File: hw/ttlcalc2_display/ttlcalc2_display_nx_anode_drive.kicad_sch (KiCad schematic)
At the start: 89 parts, among them Q26 MPSA92, Q27 MPSA92, Q28 MPSA92, Q29 MPSA92, Q30 MPSA92, Q31 MPSA42, Q32 MPSA42, Q33 MPSA42, Q34 MPSA42, Q35 MPSA42, Q36 MPSA92, Q37 MPSA92, Q38 MPSA92, Q39 MPSA92, Q40 MPSA92, Q41 MPSA42, Q42 MPSA42, Q43 MPSA42, Q44 MPSA42, Q45 MPSA42, Q46 MPSA92, Q47 MPSA92, Q48 MPSA92, Q49 MPSA92, Q50 MPSA42, Q51 MPSA42, Q52 MPSA42, Q53 MPSA42, U14 74LS04, U15 74LS138, U16 74LS138, U17 74LS04, U18 74LS04

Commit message: Continue work on display driver board schematic
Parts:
- R28: renamed from R43; footprint Resistor_THT:R_Axial_DIN0309_L9.0mm_D3.2mm_P2.54mm_Vertical -> Resistor_THT:R_Axial_DIN0207_L6.3mm_D2.5mm_P2.54mm_Vertical
- R29: renamed from R63; footprint Resistor_THT:R_Axial_DIN0309_L9.0mm_D3.2mm_P2.54mm_Vertical -> Resistor_THT:R_Axial_DIN0207_L6.3mm_D2.5mm_P2.54mm_Vertical
- R30: renamed from R80; footprint Resistor_THT:R_Axial_DIN0309_L9.0mm_D3.2mm_P2.54mm_Vertical -> Resistor_THT:R_Axial_DIN0207_L6.3mm_D2.5mm_P2.54mm_Vertical
- R31: renamed from R28; footprint Resistor_THT:R_Axial_DIN0309_L9.0mm_D3.2mm_P2.54mm_Vertical -> Resistor_THT:R_Axial_DIN0207_L6.3mm_D2.5mm_P2.54mm_Vertical
- R32: renamed from R33; footprint Resistor_THT:R_Axial_DIN0309_L9.0mm_D3.2mm_P2.54mm_Vertical -> Resistor_THT:R_Axial_DIN0207_L6.3mm_D2.5mm_P2.54mm_Vertical
- R33: renamed from R48; footprint Resistor_THT:R_Axial_DIN0309_L9.0mm_D3.2mm_P2.54mm_Vertical -> Resistor_THT:R_Axial_DIN0207_L6.3mm_D2.5mm_P2.54mm_Vertical
- R34: renamed from R53; footprint Resistor_THT:R_Axial_DIN0309_L9.0mm_D3.2mm_P2.54mm_Vertical -> Resistor_THT:R_Axial_DIN0207_L6.3mm_D2.5mm_P2.54mm_Vertical
- R35: renamed from R68; footprint Resistor_THT:R_Axial_DIN0309_L9.0mm_D3.2mm_P2.54mm_Vertical -> Resistor_THT:R_Axial_DIN0207_L6.3mm_D2.5mm_P2.54mm_Vertical
- R36: renamed from R72; footprint Resistor_THT:R_Axial_DIN0309_L9.0mm_D3.2mm_P2.54mm_Vertical -> Resistor_THT:R_Axial_DIN0207_L6.3mm_D2.5mm_P2.54mm_Vertical
- R37: renamed from R38; footprint Resistor_THT:R_Axial_DIN0309_L9.0mm_D3.2mm_P2.54mm_Vertical -> Resistor_THT:R_Axial_DIN0207_L6.3mm_D2.5mm_P2.54mm_Vertical
- R38: renamed from R58; footprint Resistor_THT:R_Axial_DIN0309_L9.0mm_D3.2mm_P2.54mm_Vertical -> Resistor_THT:R_Axial_DIN0207_L6.3mm_D2.5mm_P2.54mm_Vertical
- R39: renamed from R76; footprint Resistor_THT:R_Axial_DIN0309_L9.0mm_D3.2mm_P2.54mm_Vertical -> Resistor_THT:R_Axial_DIN0207_L6.3mm_D2.5mm_P2.54mm_Vertical
- R40: renamed from R44; footprint Resistor_THT:R_Axial_DIN0309_L9.0mm_D3.2mm_P2.54mm_Vertical -> Resistor_THT:R_Axial_DIN0207_L6.3mm_D2.5mm_P2.54mm_Vertical
- R41: renamed from R64; footprint Resistor_THT:R_Axial_DIN0309_L9.0mm_D3.2mm_P2.54mm_Vertical -> Resistor_THT:R_Axial_DIN0207_L6.3mm_D2.5mm_P2.54mm_Vertical
- R42: renamed from R81; footprint Resistor_THT:R_Axial_DIN0309_L9.0mm_D3.2mm_P2.54mm_Vertical -> Resistor_THT:R_Axial_DIN0207_L6.3mm_D2.5mm_P2.54mm_Vertical
- R43: renamed from R29; footprint Resistor_THT:R_Axial_DIN0309_L9.0mm_D3.2mm_P2.54mm_Vertical -> Resistor_THT:R_Axial_DIN0207_L6.3mm_D2.5mm_P2.54mm_Vertical
- R44: renamed from R34; footprint Resistor_THT:R_Axial_DIN0309_L9.0mm_D3.2mm_P2.54mm_Vertical -> Resistor_THT:R_Axial_DIN0207_L6.3mm_D2.5mm_P2.54mm_Vertical
- R45: renamed from R49; footprint Resistor_THT:R_Axial_DIN0309_L9.0mm_D3.2mm_P2.54mm_Vertical -> Resistor_THT:R_Axial_DIN0207_L6.3mm_D2.5mm_P2.54mm_Vertical
- R46: renamed from R54; footprint Resistor_THT:R_Axial_DIN0309_L9.0mm_D3.2mm_P2.54mm_Vertical -> Resistor_THT:R_Axial_DIN0207_L6.3mm_D2.5mm_P2.54mm_Vertical
- R47: renamed from R69; footprint Resistor_THT:R_Axial_DIN0309_L9.0mm_D3.2mm_P2.54mm_Vertical -> Resistor_THT:R_Axial_DIN0207_L6.3mm_D2.5mm_P2.54mm_Vertical
- R48: renamed from R73; footprint Resistor_THT:R_Axial_DIN0309_L9.0mm_D3.2mm_P2.54mm_Vertical -> Resistor_THT:R_Axial_DIN0207_L6.3mm_D2.5mm_P2.54mm_Vertical
- R49: renamed from R39; footprint Resistor_THT:R_Axial_DIN0309_L9.0mm_D3.2mm_P2.54mm_Vertical -> Resistor_THT:R_Axial_DIN0207_L6.3mm_D2.5mm_P2.54mm_Vertical
- R50: renamed from R59; footprint Resistor_THT:R_Axial_DIN0309_L9.0mm_D3.2mm_P2.54mm_Vertical -> Resistor_THT:R_Axial_DIN0207_L6.3mm_D2.5mm_P2.54mm_Vertical
- R51: renamed from R77; footprint Resistor_THT:R_Axial_DIN0309_L9.0mm_D3.2mm_P2.54mm_Vertical -> Resistor_THT:R_Axial_DIN0207_L6.3mm_D2.5mm_P2.54mm_Vertical
- R52: renamed from R45; footprint Resistor_THT:R_Axial_DIN0309_L9.0mm_D3.2mm_P2.54mm_Vertical -> Resistor_THT:R_Axial_DIN0207_L6.3mm_D2.5mm_P2.54mm_Vertical
- R53: renamed from R65; footprint Resistor_THT:R_Axial_DIN0309_L9.0mm_D3.2mm_P2.54mm_Vertical -> Resistor_THT:R_Axial_DIN0207_L6.3mm_D2.5mm_P2.54mm_Vertical
- R54: renamed from R82; footprint Resistor_THT:R_Axial_DIN0309_L9.0mm_D3.2mm_P2.54mm_Vertical -> Resistor_THT:R_Axial_DIN0207_L6.3mm_D2.5mm_P2.54mm_Vertical
- R55: renamed from R30; footprint Resistor_THT:R_Axial_DIN0309_L9.0mm_D3.2mm_P2.54mm_Vertical -> Resistor_THT:R_Axial_DIN0207_L6.3mm_D2.5mm_P2.54mm_Vertical
- R56: renamed from R35; footprint Resistor_THT:R_Axial_DIN0309_L9.0mm_D3.2mm_P2.54mm_Vertical -> Resistor_THT:R_Axial_DIN0207_L6.3mm_D2.5mm_P2.54mm_Vertical
- R57: renamed from R50; footprint Resistor_THT:R_Axial_DIN0309_L9.0mm_D3.2mm_P2.54mm_Vertical -> Resistor_THT:R_Axial_DIN0207_L6.3mm_D2.5mm_P2.54mm_Vertical
- R58: renamed from R55; footprint Resistor_THT:R_Axial_DIN0309_L9.0mm_D3.2mm_P2.54mm_Vertical -> Resistor_THT:R_Axial_DIN0207_L6.3mm_D2.5mm_P2.54mm_Vertical
- R59: renamed from R70; footprint Resistor_THT:R_Axial_DIN0309_L9.0mm_D3.2mm_P2.54mm_Vertical -> Resistor_THT:R_Axial_DIN0207_L6.3mm_D2.5mm_P2.54mm_Vertical
- R60: renamed from R74; footprint Resistor_THT:R_Axial_DIN0309_L9.0mm_D3.2mm_P2.54mm_Vertical -> Resistor_THT:R_Axial_DIN0207_L6.3mm_D2.5mm_P2.54mm_Vertical
- R61: renamed from R40; footprint Resistor_THT:R_Axial_DIN0309_L9.0mm_D3.2mm_P2.54mm_Vertical -> Resistor_THT:R_Axial_DIN0207_L6.3mm_D2.5mm_P2.54mm_Vertical
- R62: renamed from R60; footprint Resistor_THT:R_Axial_DIN0309_L9.0mm_D3.2mm_P2.54mm_Vertical -> Resistor_THT:R_Axial_DIN0207_L6.3mm_D2.5mm_P2.54mm_Vertical
- R63: renamed from R78; footprint Resistor_THT:R_Axial_DIN0309_L9.0mm_D3.2mm_P2.54mm_Vertical -> Resistor_THT:R_Axial_DIN0207_L6.3mm_D2.5mm_P2.54mm_Vertical
- R64: renamed from R46; footprint Resistor_THT:R_Axial_DIN0309_L9.0mm_D3.2mm_P2.54mm_Vertical -> Resistor_THT:R_Axial_DIN0207_L6.3mm_D2.5mm_P2.54mm_Vertical
- R65: renamed from R66; footprint Resistor_THT:R_Axial_DIN0309_L9.0mm_D3.2mm_P2.54mm_Vertical -> Resistor_THT:R_Axial_DIN0207_L6.3mm_D2.5mm_P2.54mm_Vertical
- R66: renamed from R83; footprint Resistor_THT:R_Axial_DIN0309_L9.0mm_D3.2mm_P2.54mm_Vertical -> Resistor_THT:R_Axial_DIN0207_L6.3mm_D2.5mm_P2.54mm_Vertical
- R67: renamed from R31; footprint Resistor_THT:R_Axial_DIN0309_L9.0mm_D3.2mm_P2.54mm_Vertical -> Resistor_THT:R_Axial_DIN0207_L6.3mm_D2.5mm_P2.54mm_Vertical
- R68: renamed from R36; footprint Resistor_THT:R_Axial_DIN0309_L9.0mm_D3.2mm_P2.54mm_Vertical -> Resistor_THT:R_Axial_DIN0207_L6.3mm_D2.5mm_P2.54mm_Vertical
- R69: renamed from R51; footprint Resistor_THT:R_Axial_DIN0309_L9.0mm_D3.2mm_P2.54mm_Vertical -> Resistor_THT:R_Axial_DIN0207_L6.3mm_D2.5mm_P2.54mm_Vertical
- R70: renamed from R56; footprint Resistor_THT:R_Axial_DIN0309_L9.0mm_D3.2mm_P2.54mm_Vertical -> Resistor_THT:R_Axial_DIN0207_L6.3mm_D2.5mm_P2.54mm_Vertical
- R71: footprint Resistor_THT:R_Axial_DIN0309_L9.0mm_D3.2mm_P2.54mm_Vertical -> Resistor_THT:R_Axial_DIN0207_L6.3mm_D2.5mm_P2.54mm_Vertical
- R72: renamed from R75; footprint Resistor_THT:R_Axial_DIN0309_L9.0mm_D3.2mm_P2.54mm_Vertical -> Resistor_THT:R_Axial_DIN0207_L6.3mm_D2.5mm_P2.54mm_Vertical
- R73: renamed from R41; footprint Resistor_THT:R_Axial_DIN0309_L9.0mm_D3.2mm_P2.54mm_Vertical -> Resistor_THT:R_Axial_DIN0207_L6.3mm_D2.5mm_P2.54mm_Vertical
- R74: renamed from R61; footprint Resistor_THT:R_Axial_DIN0309_L9.0mm_D3.2mm_P2.54mm_Vertical -> Resistor_THT:R_Axial_DIN0207_L6.3mm_D2.5mm_P2.54mm_Vertical
- R75: renamed from R79; footprint Resistor_THT:R_Axial_DIN0309_L9.0mm_D3.2mm_P2.54mm_Vertical -> Resistor_THT:R_Axial_DIN0207_L6.3mm_D2.5mm_P2.54mm_Vertical
- R76: renamed from R47; footprint Resistor_THT:R_Axial_DIN0309_L9.0mm_D3.2mm_P2.54mm_Vertical -> Resistor_THT:R_Axial_DIN0207_L6.3mm_D2.5mm_P2.54mm_Vertical
- R77: renamed from R67; footprint Resistor_THT:R_Axial_DIN0309_L9.0mm_D3.2mm_P2.54mm_Vertical -> Resistor_THT:R_Axial_DIN0207_L6.3mm_D2.5mm_P2.54mm_Vertical
- R78: renamed from R32; footprint Resistor_THT:R_Axial_DIN0309_L9.0mm_D3.2mm_P2.54mm_Vertical -> Resistor_THT:R_Axial_DIN0207_L6.3mm_D2.5mm_P2.54mm_Vertical
- R79: renamed from R37; footprint Resistor_THT:R_Axial_DIN0309_L9.0mm_D3.2mm_P2.54mm_Vertical -> Resistor_THT:R_Axial_DIN0207_L6.3mm_D2.5mm_P2.54mm_Vertical
- R80: renamed from R52; footprint Resistor_THT:R_Axial_DIN0309_L9.0mm_D3.2mm_P2.54mm_Vertical -> Resistor_THT:R_Axial_DIN0207_L6.3mm_D2.5mm_P2.54mm_Vertical
- R81: renamed from R57; footprint Resistor_THT:R_Axial_DIN0309_L9.0mm_D3.2mm_P2.54mm_Vertical -> Resistor_THT:R_Axial_DIN0207_L6.3mm_D2.5mm_P2.54mm_Vertical
- R82: renamed from R42; footprint Resistor_THT:R_Axial_DIN0309_L9.0mm_D3.2mm_P2.54mm_Vertical -> Resistor_THT:R_Axial_DIN0207_L6.3mm_D2.5mm_P2.54mm_Vertical
- R83: renamed from R62; footprint Resistor_THT:R_Axial_DIN0309_L9.0mm_D3.2mm_P2.54mm_Vertical -> Resistor_THT:R_Axial_DIN0207_L6.3mm_D2.5mm_P2.54mm_Vertical
- renumbered Q31 to Q26, Q41 to Q27, Q50 to Q28, Q26 to Q29, Q36 to Q30, Q46 to Q31, Q42 to Q33, Q51 to Q34, Q27 to Q35, Q37 to Q36, Q47 to Q37, Q33 to Q38, Q43 to Q39, Q52 to Q40, Q28 to Q41, Q38 to Q42, Q48 to Q43, Q34 to Q44, Q44 to Q45, Q53 to Q46, Q29 to Q47, Q39 to Q48, Q35 to Q50, Q45 to Q51, Q30 to Q52, Q40 to Q53

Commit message: Simplify display driver board, add busy light
Removed digit storage and multiplexing logic from display driver, will handle in software instead
Add driver for busy indicator
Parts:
- renumbered Q26 to Q27, Q27 to Q28, Q28 to Q29, Q29 to Q30, Q30 to Q31, Q31 to Q32, Q32 to Q33, Q33 to Q34, Q34 to Q35, Q35 to Q36, Q36 to Q37, Q37 to Q38, Q38 to Q39, Q39 to Q40, Q40 to Q41, Q41 to Q42, Q42 to Q43, Q43 to Q44, Q44 to Q45, Q45 to Q46, Q46 to Q47, Q47 to Q48, Q48 to Q49, Q49 to Q50, Q50 to Q51, Q51 to Q52, Q52 to Q53, Q53 to Q54, R28 to R27, R29 to R28, R30 to R29, R31 to R30, R32 to R31, R33 to R32, R34 to R33, R35 to R34, R36 to R35, R37 to R36, R38 to R37, R39 to R38, R40 to R39, R41 to R40, R42 to R41, R43 to R42, R44 to R43, R45 to R44, R46 to R45, R47 to R46, R48 to R47, R49 to R48, R50 to R49, R51 to R50, R52 to R51, R53 to R52, R54 to R53, R55 to R54, R56 to R55, R57 to R56, R58 to R57, R59 to R58, R60 to R59, R61 to R60, R62 to R61, R63 to R62, R64 to R63, R65 to R64, R66 to R65, R67 to R66, R68 to R67, R69 to R68, R70 to R69, R71 to R70, R72 to R71, R73 to R72, R74 to R73, R75 to R74, R76 to R75, R77 to R76, R78 to R77, R79 to R78, R80 to R79, R81 to R80, R82 to R81, R83 to R82
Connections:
- net EN2 is gone; now on net VCC: U15.6 (E3)
- net GND: no longer U16.5 (E2)
- net ~{EN1} renamed ~{EN}
- net ~{EN}: now also U16.5 (E2)

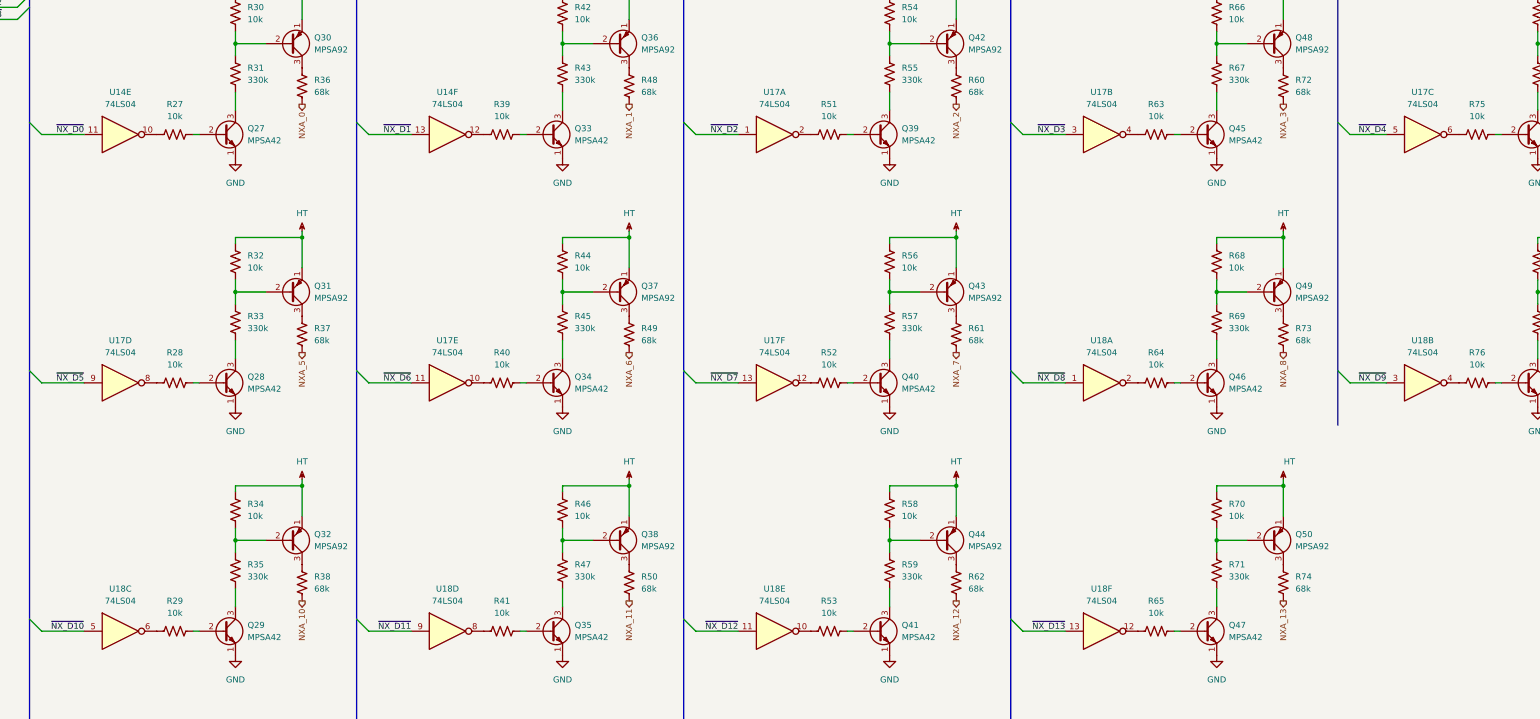
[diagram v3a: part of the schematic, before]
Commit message: Display driver board routing and silkscreen tweaks
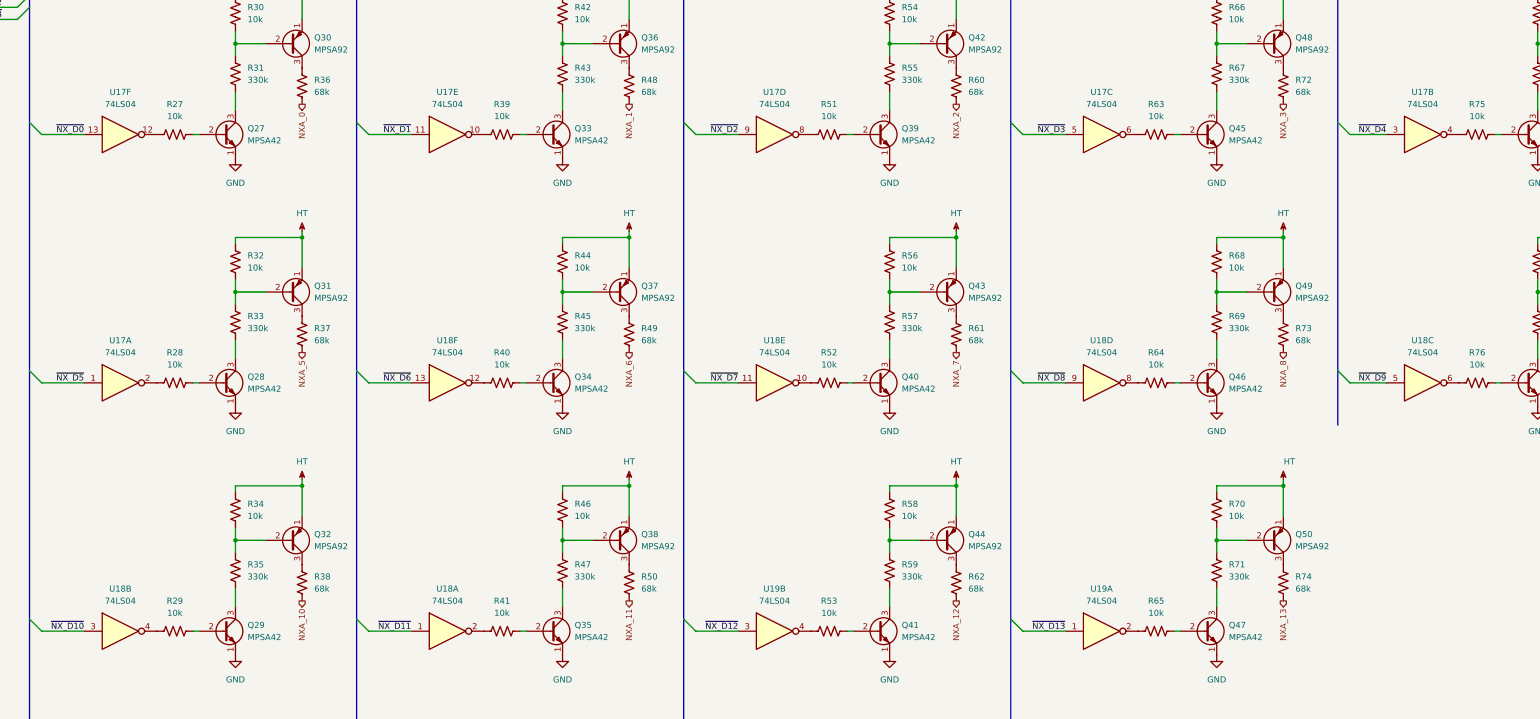
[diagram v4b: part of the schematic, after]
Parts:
- removed unit 2 of U17
- removed unit 3 of U17
- added U19: 74LS04, Package_DIP:DIP-14_W7.62mm, symbol 74xx:74LS04
- Q27, Q28, Q29, Q30, Q31, Q32, Q33, Q34, Q35, Q36, Q37, Q38, Q39, Q40, Q41, Q42, Q43, Q44, Q45, Q46, Q47, Q48, Q49, Q50, Q51, Q52, Q53, Q54: footprint Package_TO_SOT_THT:TO-92_Inline -> Package_TO_SOT_THT:TO-92_Inline_Wide
- R27, R28, R29, R30, R31, R32, R33, R34, R35, R36, R37, R38, R39, R40, R41, R42, R43, R44, R45, R46, R47, R48, R49, R50, R51, R52, R53, R54, R55, R56, R57, R58, R59, R60, R61, R62, R63, R64, R65, R66, R67, R68, R69, R70, R71, R72, R73, R74, R75, R76, R77, R78, R79, R80, R81, R82: footprint Resistor_THT:R_Axial_DIN0207_L6.3mm_D2.5mm_P2.54mm_Vertical -> Resistor_THT:R_Axial_DIN0207_L6.3mm_D2.5mm_P7.62mm_Horizontal
- renumbered U14 to U17
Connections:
- net ~{NX_D0}: now also U17.13; no longer U17.11
- net ~{NX_D10}: now also U18.3; no longer U18.5
- net ~{NX_D11}: now also U18.1; no longer U18.9
- net ~{NX_D12}: now also U19.3; no longer U18.11
- net ~{NX_D13}: now also U19.1; no longer U18.13
- net ~{NX_D1}: now also U17.11; no longer U17.13
- net ~{NX_D2}: now also U17.9; no longer U17.1
- net ~{NX_D3}: now also U17.5
- net ~{NX_D4}: now also U17.3
- net ~{NX_D5}: now also U17.1; no longer U17.9
- net ~{NX_D6}: now also U18.13; no longer U17.11
- net ~{NX_D7}: now also U18.11; no longer U17.13
- net ~{NX_D8}: now also U18.9; no longer U18.1
- net ~{NX_D9}: now also U18.5; no longer U18.3
- net at R27.1: now also U17.12; no longer U17.10
- net at R29.1: now also U18.4; no longer U18.6
- net at R76.1: now also U18.6; no longer U18.4
- net at R63.1: now also U17.6
- net at R75.1: now also U17.4
- net at R52.1: now also U18.10; no longer U17.12
- net at U18.8: now also R64.1; no longer R41.1
- net at R53.1: now also U19.4; no longer U18.10
- net at R28.1: now also U17.2; no longer U17.8
- net at R51.1: now also U17.8; no longer U17.2
- net at U18.2: now also R41.1; no longer R64.1
- net at U17.10: now also R39.1; no longer R40.1
- net at R65.1: now also U19.2; no longer U18.12
- new net: R40.1, U18.12
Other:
- moved on the sheet: U17A, U17B, U17C, U17D, U17E, U18A, U18B, U18C, U18D, U18E, U18F

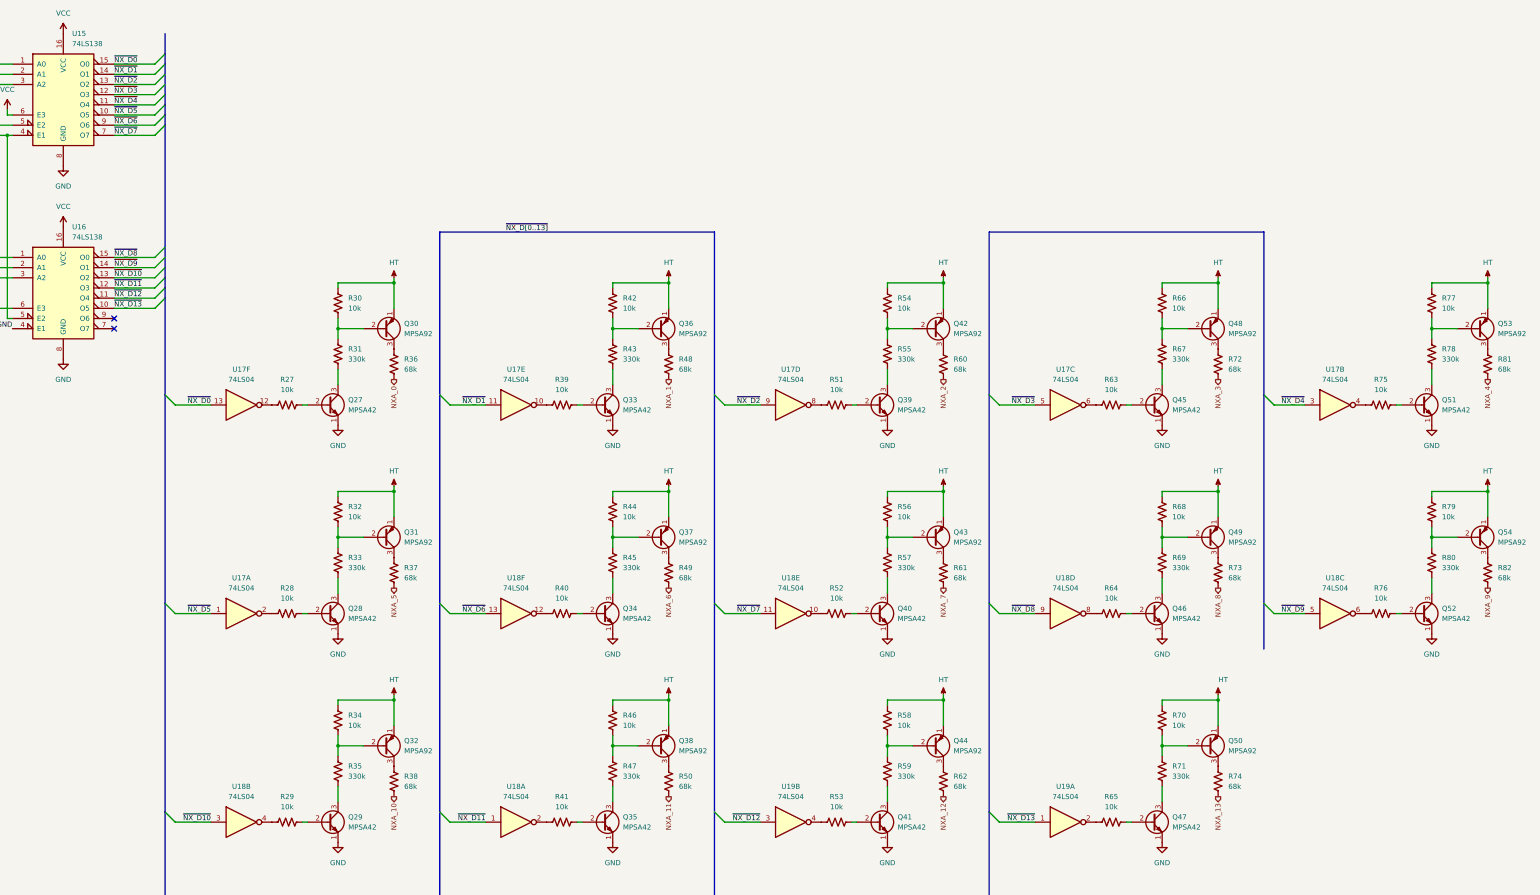
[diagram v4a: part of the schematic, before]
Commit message: Display driver geographical reannotate
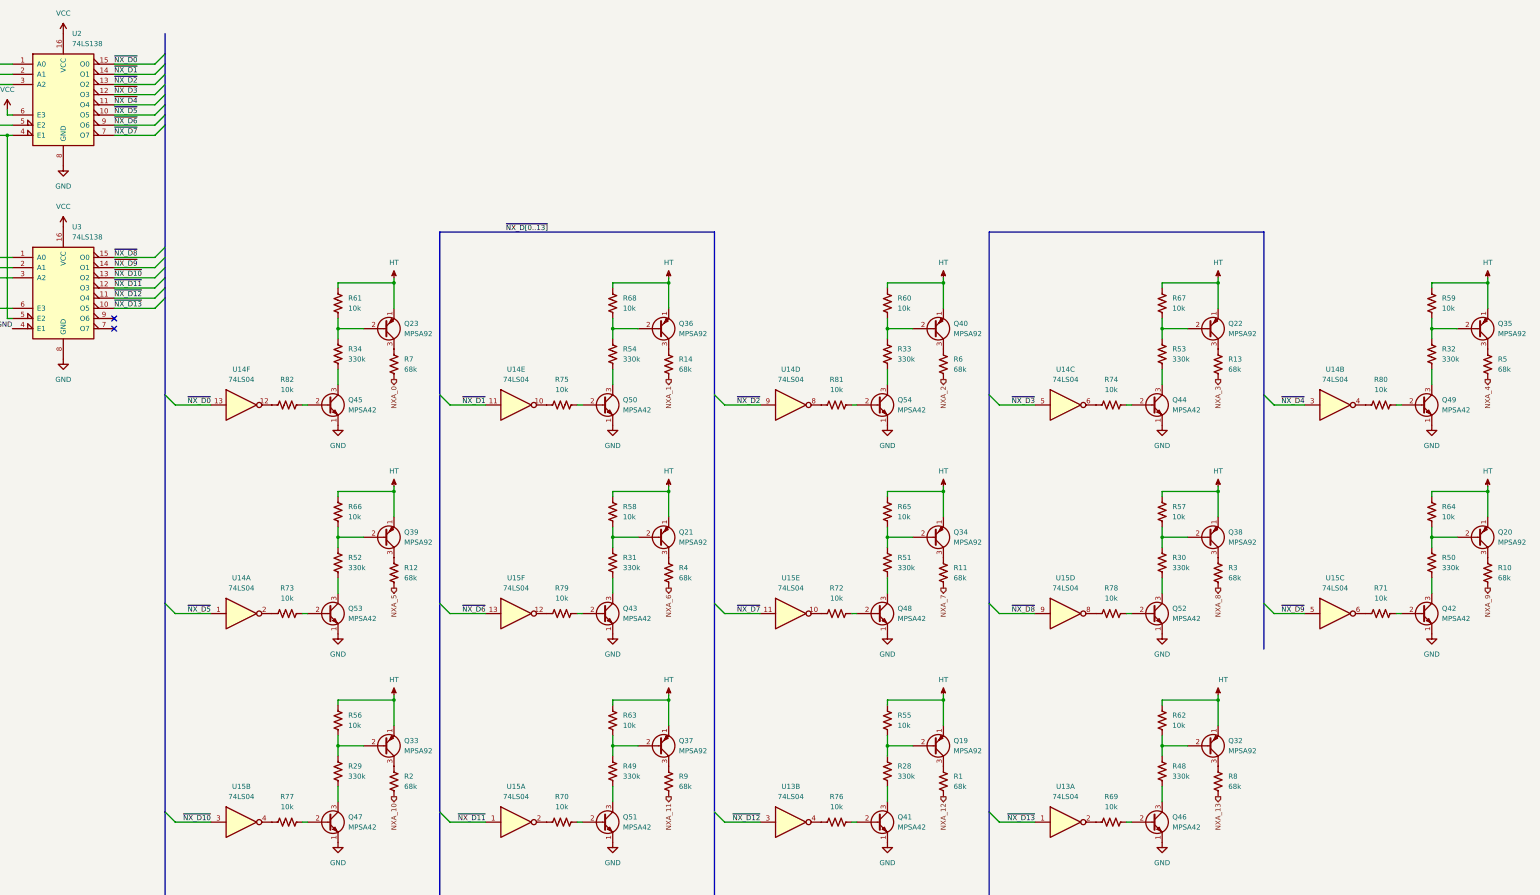
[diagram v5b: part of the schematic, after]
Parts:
- renumbered Q44 to Q19, Q54 to Q20, Q37 to Q21, Q48 to Q22, Q30 to Q23, Q50 to Q32, Q32 to Q33, Q43 to Q34, Q53 to Q35, Q38 to Q37, Q49 to Q38, Q31 to Q39, Q42 to Q40, Q52 to Q42, Q34 to Q43, Q45 to Q44, Q27 to Q45, Q47 to Q46, Q29 to Q47, Q40 to Q48, Q51 to Q49, Q33 to Q50, Q35 to Q51, Q46 to Q52, Q28 to Q53, Q39 to Q54, R62 to R1, R82 to R10, R61 to R11, R37 to R12, R72 to R13, R48 to R14, R38 to R2, R59 to R28, R35 to R29, R73 to R3, R69 to R30, R45 to R31, R78 to R32, R55 to R33, R31 to R34, R49 to R4, R71 to R48, R47 to R49, R81 to R5, R80 to R50, R57 to R51, R33 to R52, R67 to R53, R43 to R54, R58 to R55, R34 to R56, R68 to R57, R44 to R58, R77 to R59, R60 to R6, R54 to R60, R30 to R61, R70 to R62, R46 to R63, R79 to R64, R56 to R65, R32 to R66, R66 to R67, R42 to R68, R65 to R69, R36 to R7, R41 to R70, R76 to R71, R52 to R72, R28 to R73, R63 to R74, R39 to R75, R53 to R76, R29 to R77, R64 to R78, R40 to R79, R74 to R8, R75 to R80, R51 to R81, R27 to R82, R50 to R9, U19 to U13, U17 to U14, U18 to U15, U15 to U2, U16 to U3
